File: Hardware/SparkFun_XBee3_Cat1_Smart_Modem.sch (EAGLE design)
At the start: 64 parts, among them J4 QWIIC_RIGHT_ANGLE, Q2 3.1A/30V/105mΩ, U1 FSUSB30MUX_MSOP10, U2 AP63203, U3 ESD Diode, U5 ESD Diode, U6 CP210X

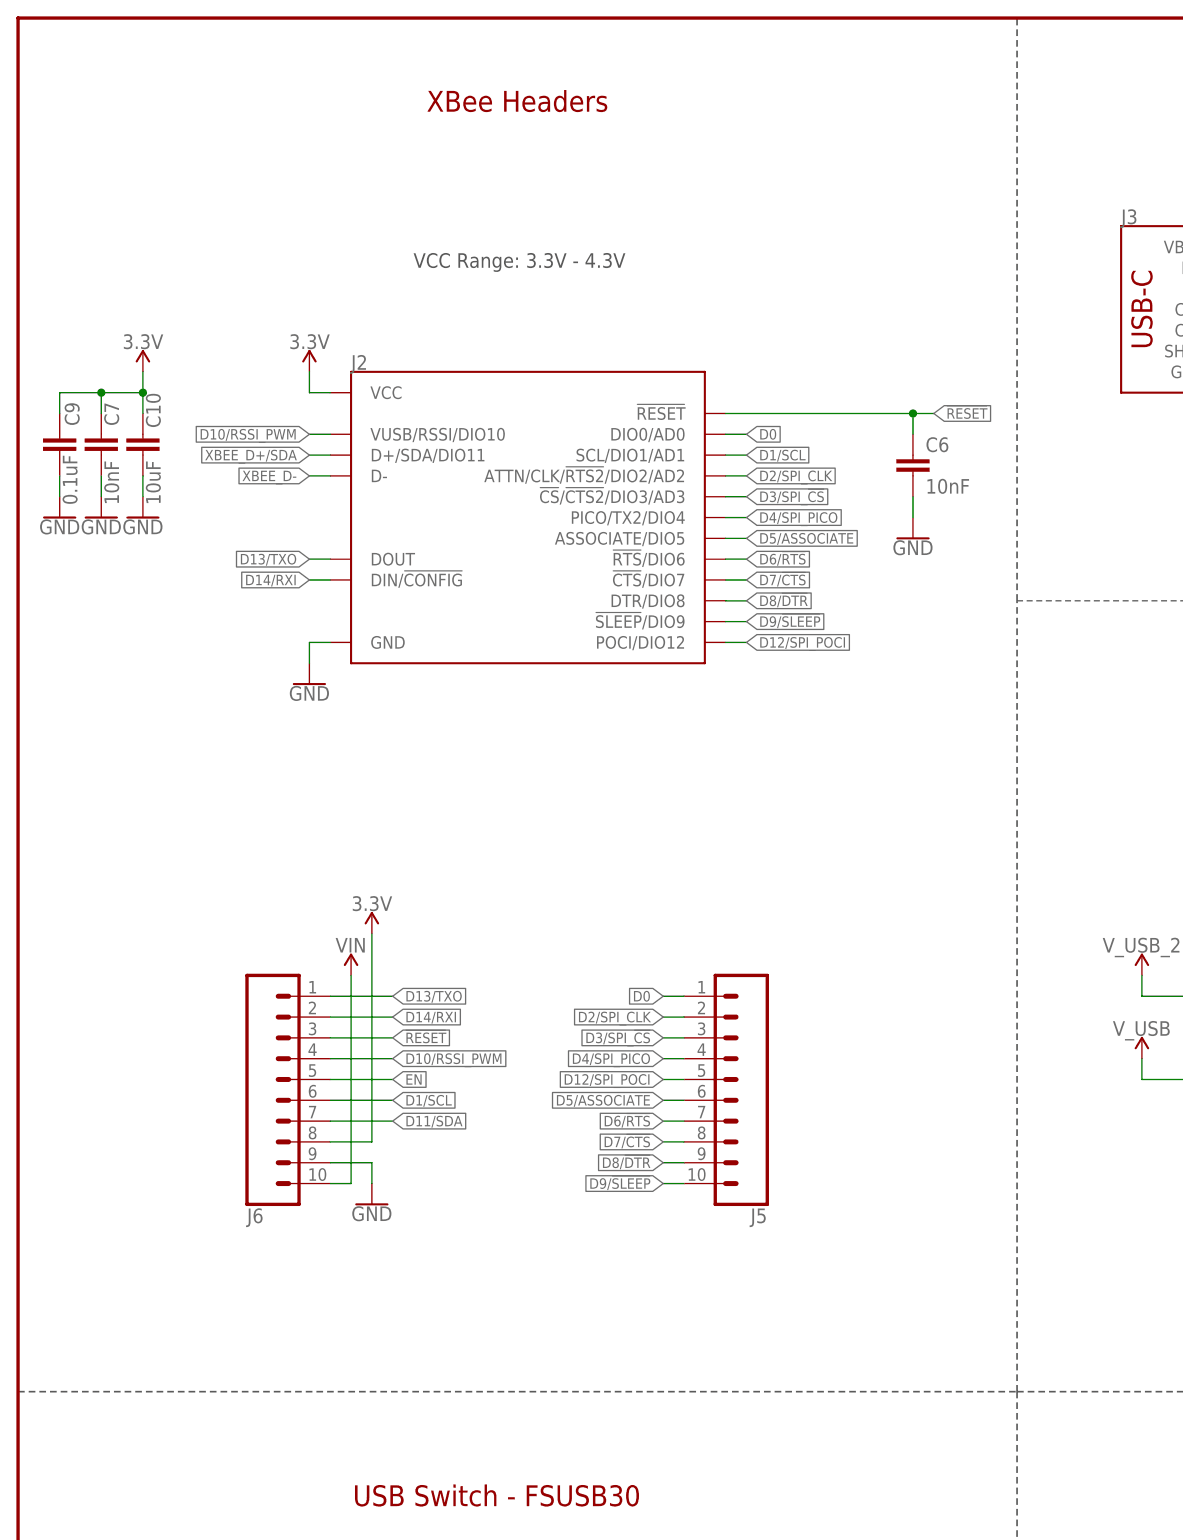
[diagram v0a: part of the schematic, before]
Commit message: Updates xbee sybmol to include pin numbers
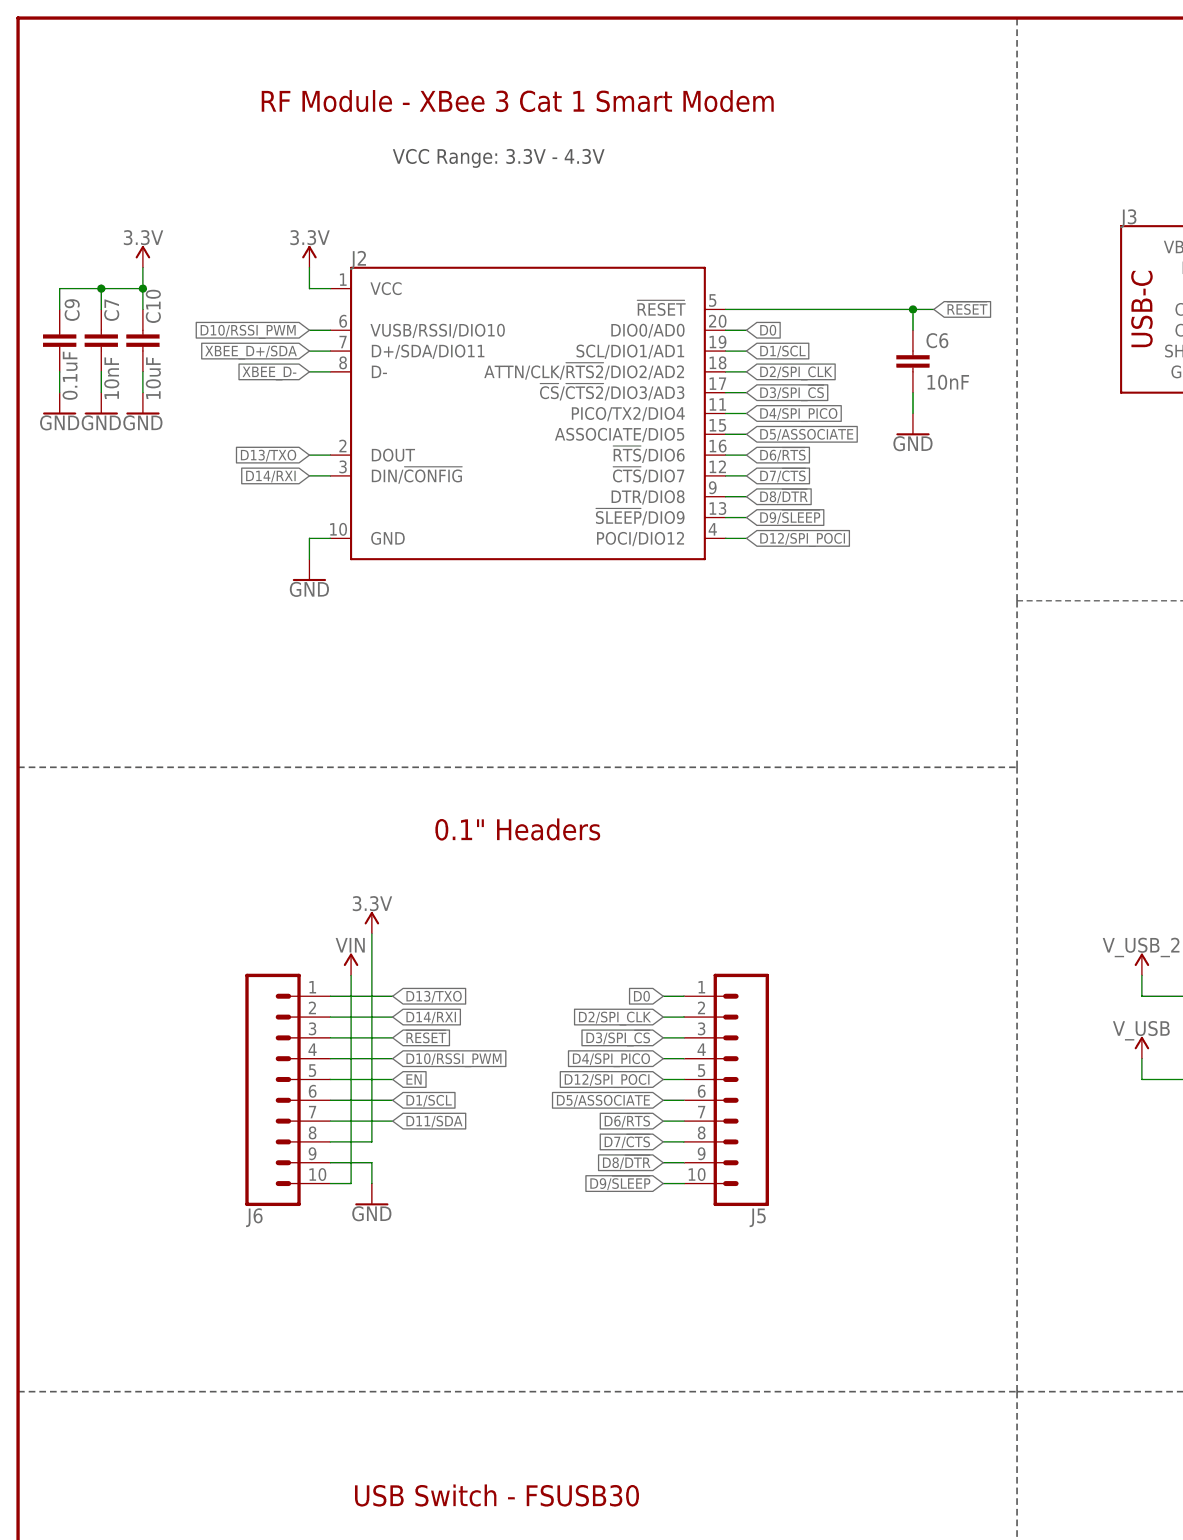
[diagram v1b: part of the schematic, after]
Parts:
- J2: device xbee_improved:XBEE_UPDATEXBEE_SMD -> xbee_smart_modem:XBEE_UPDATEXBEE_SMD
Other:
- note added: "0.1" Headers"
- note added: "RF Module - XBee 3 Cat 1 Smart Modem"
- note removed: "XBee Headers"
- moved on the sheet: C10, C6, C7, C9

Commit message: Updates library to include a version of the module with silk
* Replaces module in design with the silk-ed version
* Extends board to be able to include the module's outline in silk
* Moves buttons and through holes to fit new size
* Changes name of the product to "Xbee 3 Dev Kit"
* Moves switch to make space for new silk
* Adds RSSI LED
* Rolls version to v02
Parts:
- added D4: BLUE, SparkFun-LED:LED-BLUE0603
- added R2: 2.2k, SparkFun-Resistors:2.2KOHM-0603-1/10W-1%
- added RLED: JUMPER-SMT_2_NC_TRACE_SILK, SparkFun-Jumpers:JUMPER-SMT_2_NC_TRACE_SILK
- J2: device xbee_smart_modem:XBEE_UPDATEXBEE_SMD -> xbee_smart_modem:XBEE_UPDATEXBEE_SMD_SILK
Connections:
- net N$3 renamed FIRMWARE
- new net N$2: D4.A, R2.2
- new net N$3: D4.C, RLED.2
- net D10/RSSI_PWM: now also R2.1
- net GND: now also RLED.1
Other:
- note added: "v02"
- note removed: "v01"
- moved on the sheet: ALED, D2, D3, PLED, R11, R12, S1, S2

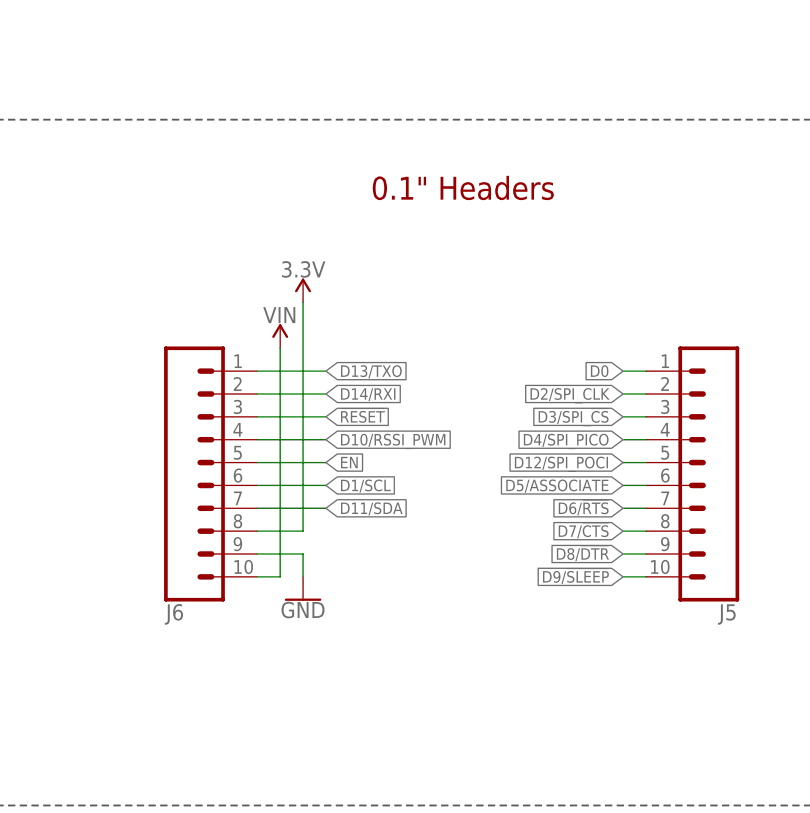
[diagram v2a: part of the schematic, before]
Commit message: NEW PINOUT - rearranges pinout to match module pinout directly
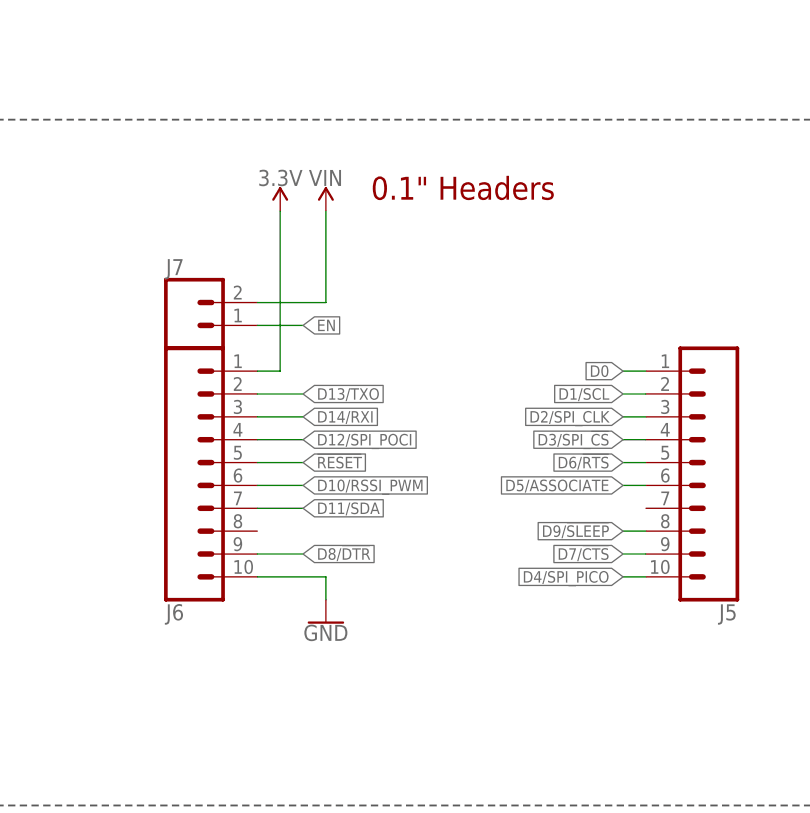
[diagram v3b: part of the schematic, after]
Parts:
- added J7: (no value), SparkFun-Connectors:CONN_021X02_NO_SILK
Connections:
- net !RESET!: now also J6.5; no longer J6.3
- net 3.3V: now also J6.1; no longer J6.8
- net D1/SCL: now also J5.2; no longer J6.6
- net D10/RSSI_PWM: now also J6.6; no longer J6.4
- net D12/SPI_POCI: now also J6.4; no longer J5.5
- net D13/TXO: now also J6.2; no longer J6.1
- net D14/RXI: now also J6.3; no longer J6.2
- net D2/SPI_CLK: now also J5.3; no longer J5.2
- net D3/SPI_!CS!: now also J5.4; no longer J5.3
- net D4/SPI_PICO: now also J5.10; no longer J5.4
- net D6/!RTS!: now also J5.5; no longer J5.7
- net D7/!CTS!: now also J5.9; no longer J5.8
- net D8/!DTR!: now also J6.9; no longer J5.9
- net D9/!SLEEP!: now also J5.8; no longer J5.10
- net EN: now also J7.1; no longer J6.5
- net GND: now also J6.10; no longer J6.9
- net VIN: now also J7.2; no longer J6.10

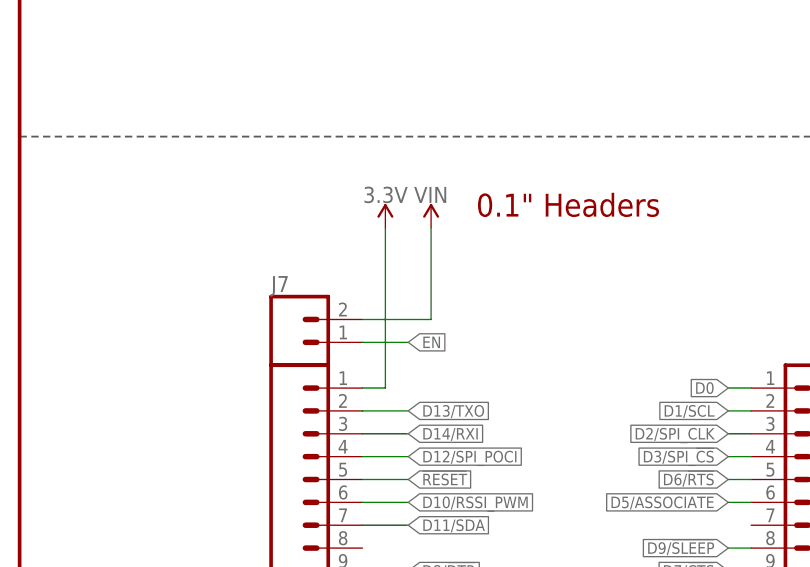
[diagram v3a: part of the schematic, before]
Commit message: Updates silk
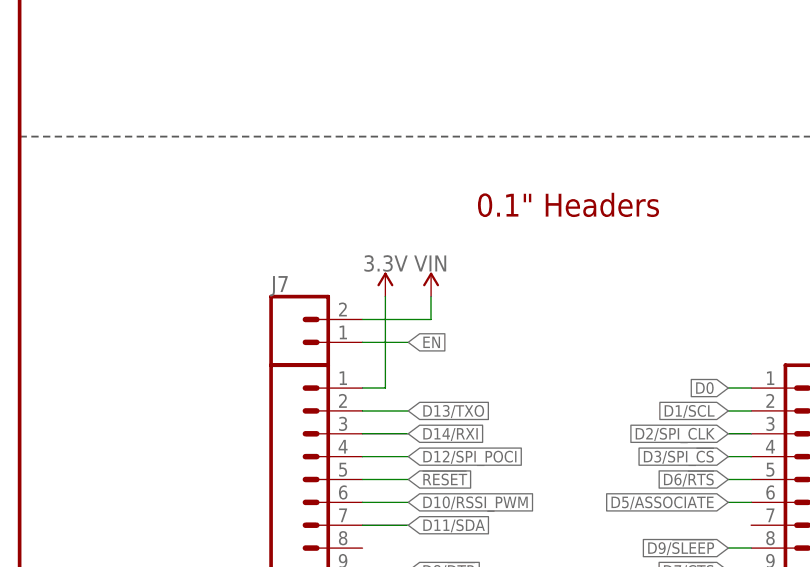
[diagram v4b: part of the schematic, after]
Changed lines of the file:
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@@
 <attribute name="NAME" x="299.72" y="42.672" size="1.778" layer="95" font="vector" rot="R180" align="center"/>
 </instance>
-<instance part="SUPPLY23" gate="G$1" x="40.64" y="177.8" smashed="yes">
-<attribute name="VALUE" x="40.64" y="180.594" size="1.778" layer="96" font="vector" align="bottom-center"/>
+<instance part="SUPPLY23" gate="G$1" x="40.64" y="170.18" smashed="yes">
+<attribute name="VALUE" x="40.64" y="172.974" size="1.778" layer="96" font="vector" align="bottom-center"/>
 </instance>
-<instance part="SUPPLY24" gate="G$1" x="45.72" y="177.8" smashed="yes">
-<attribute name="VALUE" x="45.72" y="180.594" size="1.778" layer="96" font="vector" align="bottom-center"/>
+<instance part="SUPPLY24" gate="G$1" x="45.72" y="170.18" smashed="yes">
+<attribute name="VALUE" x="45.72" y="172.974" size="1.778" layer="96" font="vector" align="bottom-center"/>
 </instance>
 <instance part="GND17" gate="1" x="45.72" y="132.08" smashed="yes" rot="MR0">
@@
 </segment>
 <segment>
-<wire x1="40.64" y1="160.02" x2="40.64" y2="177.8" width="0.1524" layer="91"/>
+<wire x1="40.64" y1="160.02" x2="40.64" y2="170.18" width="0.1524" layer="91"/>
 <wire x1="38.1" y1="160.02" x2="40.64" y2="160.02" width="0.1524" layer="91"/>
 <pinref part="SUPPLY23" gate="G$1" pin="3.3V"/>
@@
 <segment>
 <wire x1="38.1" y1="167.64" x2="45.72" y2="167.64" width="0.1524" layer="91"/>
-<wire x1="45.72" y1="167.64" x2="45.72" y2="177.8" width="0.1524" layer="91"/>
+<wire x1="45.72" y1="167.64" x2="45.72" y2="170.18" width="0.1524" layer="91"/>
 <pinref part="SUPPLY24" gate="G$1" pin="VIN"/>
 <pinref part="J7" gate="G$1" pin="2"/>

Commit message: Replaces USB-C connector with four layer footprint
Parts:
- J1, J3: value (none) -> USB Female Type C Connector; device SparkFun-Connectors:USB_C_2-LAYER_PADS -> SparkFun-Connectors:USB_C_4-LAYER-ISOLATED
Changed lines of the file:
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@@
 <part name="R15" library="SparkFun-Resistors" deviceset="2.2KOHM" device="-0603-1/10W-1%" value="2.2k"/>
 <part name="SUPPLY29" library="SparkFun-PowerSymbols" deviceset="3.3V" device=""/>
-<part name="J3" library="SparkFun-Connectors" deviceset="USB_C" device="_2-LAYER_PADS"/>
+<part name="J3" library="SparkFun-Connectors" deviceset="USB_C" device="_4-LAYER-ISOLATED" value="USB Female Type C Connector"/>
 <part name="GND4" library="SparkFun-PowerSymbols" deviceset="GND" device=""/>
 <part name="R7" library="SparkFun-Resistors" deviceset="5.1KOHM" device="5.1KOHM-0603-1/10W-1%" value="5.1k"/>
@@
 <part name="GND22" library="SparkFun-PowerSymbols" deviceset="GND" device=""/>
 <part name="SUPPLY10" library="SparkFun-PowerSymbols" deviceset="3.3V" device=""/>
-<part name="J1" library="SparkFun-Connectors" deviceset="USB_C" device="_2-LAYER_PADS"/>
+<part name="J1" library="SparkFun-Connectors" deviceset="USB_C" device="_4-LAYER-ISOLATED" value="USB Female Type C Connector"/>
 <part name="GND23" library="SparkFun-PowerSymbols" deviceset="GND" device=""/>
 <part name="R13" library="SparkFun-Resistors" deviceset="5.1KOHM" device="5.1KOHM-0603-1/10W-1%" value="5.1k"/>
@@
 </instance>
 <instance part="J3" gate="J1" x="137.16" y="243.84" smashed="yes">
-<attribute name="VALUE" x="134.62" y="231.394" size="1.778" layer="96" font="vector" rot="MR180" align="top-left"/>
 <attribute name="NAME" x="134.62" y="254.254" size="1.778" layer="95" font="vector"/>
 </instance>
@@
 </instance>
 <instance part="J1" gate="J1" x="226.06" y="243.84" smashed="yes">
-<attribute name="VALUE" x="223.52" y="231.394" size="1.778" layer="96" font="vector" rot="MR180" align="top-left"/>
 <attribute name="NAME" x="223.52" y="254.254" size="1.778" layer="95" font="vector"/>
 </instance>

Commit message: Updates title for USB-C section
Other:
- note added: "USB to UART Bridge - CP2104/2N"
- note removed: "USB-C and USB to UART Bridge - (CP2104/2N)"
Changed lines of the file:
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@@
 <plain>
 <text x="45.72" y="261.62" size="1.778" layer="97" font="vector">VCC Range: 3.3V - 4.3V</text>
-<text x="368.3" y="266.7" size="2.54" layer="94" font="vector" align="center">USB-C and USB to UART Bridge  - (CP2104/2N)</text>
+<text x="368.3" y="266.7" size="2.54" layer="94" font="vector" align="center">USB to UART Bridge  - CP2104/2N</text>
 <text x="203.454" y="197.866" size="2.54" layer="94" font="vector" align="center">Buck Converter - AP63203</text>
 <text x="360.172" y="165.1" size="2.54" layer="94" font="vector" align="center">Lipo Battery Connector</text>

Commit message: Fixes silk on modem and silk for certain through holes
* Moves "VIN" and "EN" through holes
* Moves the switch down because the above through holes moved
* Shift the copper down to accommodate smaller XBee modules
* Changes name to "Development Board"
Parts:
- removed J7: (no value), SparkFun-Connectors:CONN_021X02_NO_SILK
- added J10, J9: (no value), SparkFun-Connectors:CONN_01PTH_NO_SILK_YES_STOP
- added R4: 10k, SparkFun-Resistors:10KOHM-0603-1/10W-1%
- J2: device xbee_smart_modem:XBEE_UPDATEXBEE_SMD_SILK -> xbee_smart_modem:XBEE_UPDATEXBEE_SMD
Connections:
- net !RESET!: now also R4.1
- net 3.3V: now also R4.2
- net D7/!CTS!: now also U6.CTS
- net EN: now also J10.1; no longer J7.1
- net VIN: now also J9.1; no longer J7.2

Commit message: Moves resistor for LEDs so that they're grouped in a better configuration
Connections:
- net N$21 renamed ALED
- net N$23 renamed PLED
- net N$3 renamed RLED
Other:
- note added: "v10"
- note removed: "v02"
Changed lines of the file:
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@@
 <wire x1="294.64" y1="172.72" x2="431.8" y2="172.72" width="0.2032" layer="97" style="longdash"/>
 <wire x1="121.92" y1="111.76" x2="121.92" y2="0" width="0.2032" layer="97" style="longdash"/>
-<text x="424.18" y="7.62" size="2.54" layer="94" font="vector" align="center">v02</text>
+<text x="424.18" y="7.62" size="2.54" layer="94" font="vector" align="center">v10</text>
 <text x="363.22" y="10.16" size="2.54" layer="94" font="vector" align="center">Elias Santistevan</text>
 <wire x1="223.52" y1="111.76" x2="223.52" y2="0" width="0.2032" layer="97" style="longdash"/>
@@
 </segment>
 </net>
-<net name="N$21" class="0">
+<net name="ALED" class="0">
 <segment>
 <pinref part="ALED" gate="G$1" pin="2"/>
@@
 </segment>
 </net>
-<net name="N$23" class="0">
+<net name="PLED" class="0">
 <segment>
 <pinref part="PLED" gate="G$1" pin="2"/>
@@
 </segment>
 </net>
-<net name="N$3" class="0">
+<net name="RLED" class="0">
 <segment>
 <pinref part="RLED" gate="G$1" pin="2"/>
